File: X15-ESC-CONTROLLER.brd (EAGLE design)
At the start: 100 x 80 mm, 25 parts, among them IC1 OP-AMP, J1 3V3 -SWCLK-GND-SWDIO- NRST, Y1 ECS-80-S-4X

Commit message: Board dimensions
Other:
- board size 100 x 80 mm -> 51.6 x 34.2 mm
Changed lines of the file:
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@@
 <setting verticaltext="up"/>
 </settings>
-<grid distance="50" unitdist="mil" unit="mil" style="lines" multiple="1" display="no" altdistance="5" altunitdist="mil" altunit="mil"/>
+<grid distance="1" unitdist="mil" unit="mil" style="lines" multiple="1" display="no" altdistance="5" altunitdist="mil" altunit="mil"/>
 <layers>
 <layer number="1" name="Top" color="4" fill="1" visible="yes" active="yes"/>
@@
 <board>
 <plain>
-<wire x1="0" y1="0" x2="100" y2="0" width="0" layer="20"/>
-<wire x1="100" y1="0" x2="100" y2="80" width="0" layer="20"/>
-<wire x1="100" y1="80" x2="0" y2="80" width="0" layer="20"/>
-<wire x1="0" y1="80" x2="0" y2="0" width="0" layer="20"/>
+<wire x1="0" y1="0" x2="51.562" y2="0" width="0" layer="20"/>
+<wire x1="51.562" y1="0" x2="51.6382" y2="34.1884" width="0" layer="20"/>
+<wire x1="51.6382" y1="34.1884" x2="0" y2="34.2138" width="0" layer="20"/>
+<wire x1="0" y1="34.2138" x2="0" y2="0" width="0" layer="20"/>
 </plain>
 <attributes>

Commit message: Board Edits
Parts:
- removed LED1: LAP4-BOTTOM, led:P47F-BOTTOM
- removed S1: MOMENTARY-SWITCH-SPST-PTH-6.0MM, SparkFun-Switches:TACTILE_SWITCH_PTH_6.0MM
- added D1: COLOR, LED, 0805:0805
- added J2, J4: (no value), SparkFun-Connectors:1X06_NO_SILK
- added U$7: (no value), OTHER, Push button - FSM2JMTR:DISCRETECOMPONENTS_SW_2512
- J1: device X15-Parts-Library:1X05 -> X15-ESC-Controller-Parts-Library:1X05
- J3: device SparkFun-Connectors:1X10 -> SparkFun-Connectors:1X06_NO_SILK
- U$1: device X15-Parts-Library:STM32F042K6T6 -> X15-ESC-Controller-Parts-Library:STM32F042K6T6
- U$2: device X15-Parts-Library:TCAN337D -> X15-ESC-Controller-Parts-Library:TCAN337D
- U$3, U$4, U$6: device X15-Parts-Library:JST_8_PIN -> X15-ESC-Controller-Parts-Library:JST_8_PIN
- U$5: device X15-Parts-Library:BACKPLANE_CONNECTOR -> X15-ESC-Controller-Parts-Library:BACKPLANE_CONNECTORS_BKP
- Y1: device X15-Parts-Library:XTAL_ECS-80-S-4X -> X15-ESC-Controller-Parts-Library:XTAL_ECS-80-S-4X
- moved JP1 91.1 mm to (46.5, 23.4)
- moved U$2 84.7 mm to (43.9, 8.78)
- moved Y1 74.6 mm to (35.9, 5.23)
- moved C3 72.9 mm to (9.40, 2.79)
- moved U$5 72.0 mm to (42.7, 29.2), turned to 90 degrees
- moved U$1 71.5 mm to (23.8, 23.9)
- moved IC1 69.3 mm to (47.5, 17.3)
- moved C2 68.0 mm to (9.40, 5.84)
- moved C8 67.2 mm to (10.9, 11.4)
- moved R4 65.4 mm to (15.2, 8.13)
- moved U$4 64.0 mm to (41.4, 24.3)
- moved C1 63.2 mm to (9.40, 8.89)
- moved C7 63.1 mm to (8.38, 11.4)
- moved R5 60.3 mm to (9.65, 14.0)
- moved J3 59.5 mm to (3.05, 2.79), turned to 90 degrees
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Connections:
- removed net ADC: J3.1
- removed net N$1: C1.1, C2.1, U$1.VDD
- removed net N$5: C5.2, U$2.VCC
- removed net TIM1_CH4: J3.6
- removed net TIM1_CH5: J3.7
- removed net TIM1_CH6: J3.8
- removed net TIM1_CH7: J3.9
- removed net TIM1_CH8: J3.10
- net +3V3: now also C1.1, C2.1, C5.2, U$1.VDD, U$2.VCC
- net ADC_IN0: now also J4.1
- net ADC_IN1: now also J3.1
- net ADC_IN4: now also J2.1
- net GND: now also D1.C, U$7.1; no longer LED1.C, S1.1
- net N$2: now also U$7.2; no longer S1.3
- net N$8: now also D1.A; no longer LED1.A
- net TIM16_CH1: now also J2.3
- net TIM17_CH1: now also J4.6
- net TIM1_CH1: now also J4.3; no longer J3.3
- net TIM1_CH2: no longer J3.4
- net TIM1_CH3: now also J4.5; no longer J3.5
- net TIM2_CH1: now also J3.3
- net TIM2_CH2: now also J3.4, J4.4
- net TIM2_CH3: now also J3.5
- net TIM2_CH4: now also J3.6
- net TIM3_CH2: now also J2.4
- net TIM3_CH3: now also J2.5
- net TIM3_CH4: now also J2.6
- net TLM_1: now also J4.2
- net TLM_2: now also J3.2
- net TLM_3: now also J2.2
- net TLM_ESC: no longer J3.2
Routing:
- net TIM3_CH4: track 0.00 -> 8.61 mm
- net TIM3_CH3: track 0.00 -> 6.22 mm
- added copper zone on layer 1, net GND
- added copper zone on layer 16, net GND

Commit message: Intermediate Board
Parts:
- moved Y1 1.05 mm to (36.2, 4.21)
- moved J3 0.57 mm to (2.54, 3.05)
- moved J4 0.36 mm to (7.11, 31.8)
- moved U$7 0.25 mm to (23.9, 3.81)
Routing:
- net TIM2_CH1: track 0.00 -> 146.6 mm, vias 0 -> 3
- net +3V3: track 0.00 -> 79.9 mm, vias 0 -> 3
- net TIM3_CH3: track 6.22 -> 82.1 mm, vias 0 -> 5
- net TLM_2: track 0.00 -> 75.3 mm, vias 0 -> 7
- net TIM2_CH2: track 0.00 -> 75.3 mm, vias 0 -> 8
- net GND: track 0.00 -> 73.9 mm, vias 0 -> 11
- net TIM2_CH4: track 0.00 -> 69.1 mm, vias 0 -> 5
- net ADC_IN1: track 0.00 -> 65.7 mm, vias 0 -> 6
- net N$2: track 0.00 -> 56.2 mm, vias 0 -> 4
- net N$4: track 0.00 -> 53.5 mm, vias 0 -> 6
- net TIM16_CH1: track 0.00 -> 49.5 mm, vias 0 -> 2
- net ADC_IN0: track 0.00 -> 48.7 mm, vias 0 -> 2
- net TIM1_CH3: track 0.00 -> 48.4 mm, vias 0 -> 1
- net TIM3_CH2: track 0.00 -> 48.0 mm, vias 0 -> 3
- net TLM_3: track 0.00 -> 47.1 mm, vias 0 -> 6
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
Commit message: Board Traces Completed
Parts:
- moved R3 12.6 mm to (9.37, 4.95)
- moved C4 1.24 mm to (11.2, 28.7)
- moved C2 1.22 mm to (9.37, 7.06)
- moved C8 0.18 mm to (11.0, 11.3)
- moved IC1 0.14 mm to (47.4, 17.3)
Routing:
- net GND: track 73.9 -> 194.4 mm, vias 11 -> 26
- net +3V3: track 79.9 -> 132.2 mm, vias 3 -> 13
- net TIM2_CH3: track 28.0 -> 56.8 mm, vias 4 -> 5
- net N$4: track 53.5 -> 65.9 mm
- net TLM_2: track 75.3 -> 66.1 mm, vias 7 -> 10
- net N$3: track 42.8 -> 51.3 mm
- net TIM1_CH3: track 48.4 -> 56.6 mm
- net N$8: track 0.00 -> 7.38 mm
- net N$2: track 56.2 -> 62.4 mm
- net TIM3_CH2: track 48.0 -> 53.7 mm, vias 3 -> 2
- net TIM16_CH1: track 49.5 -> 53.7 mm
- net TLM_1: track 39.1 -> 42.3 mm
- net TIM3_CH4: track 36.8 -> 39.7 mm
- net SWDIO: track 31.2 -> 33.8 mm
- net ADC_IN1: track 65.7 -> 68.2 mm
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
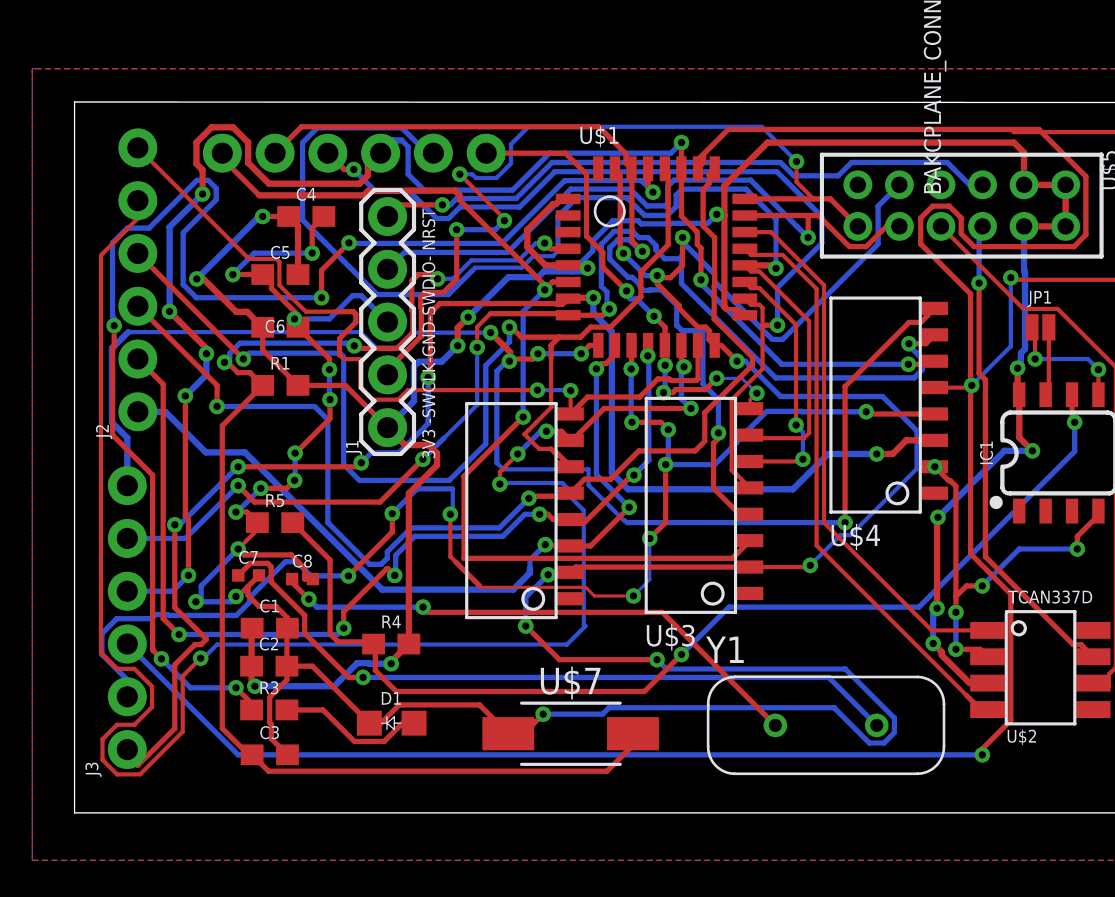
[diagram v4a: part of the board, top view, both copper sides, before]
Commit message: FIxed DRC
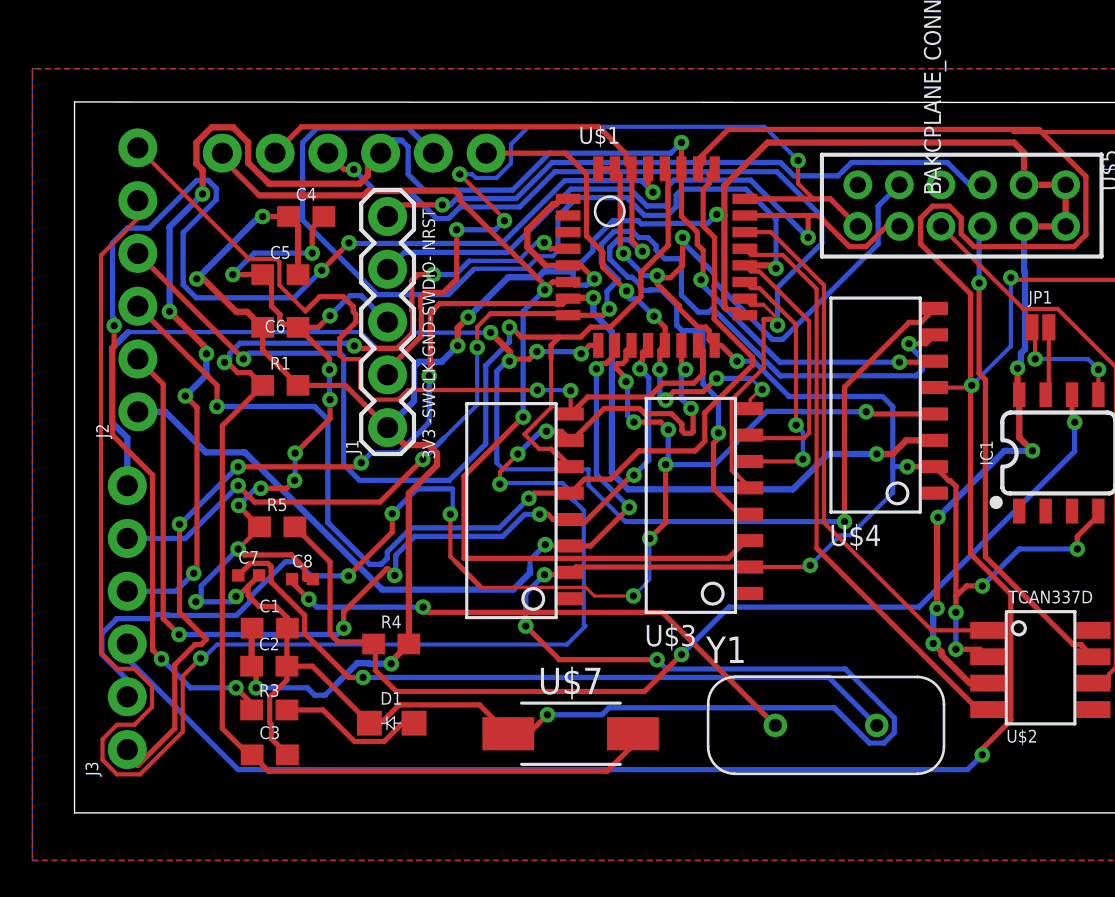
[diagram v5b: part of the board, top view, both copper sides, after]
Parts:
- moved R5 0.23 mm to (9.75, 13.8)
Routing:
- net TIM3_CH3: track 83.8 -> 85.8 mm
- net +3V3: track 132.2 -> 134.1 mm
- net TIM17_CH1: track 23.6 -> 24.8 mm
- net TIM2_CH1: track 146.6 -> 147.6 mm
- net N$4: track 65.9 -> 65.0 mm
- net TIM1_CH1: track 44.4 -> 45.2 mm
- net TIM2_CH3: track 56.8 -> 57.4 mm
- net TLM_2: track 66.1 -> 66.6 mm
- net TIM3_CH4: track 39.7 -> 40.2 mm
- net TIM2_CH2: track 75.4 -> 75.9 mm

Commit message: Final Board Edits
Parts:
- removed J4: (no value), SparkFun-Connectors:1X06_NO_SILK
- added D2: COLOR, LED, 0805:0805
- added R2: 150, SparkFun-Resistors:0603
- U$3, U$4, U$6: device X15-ESC-Controller-Parts-Library:JST_8_PIN -> X15-Parts-Library:8PIN_CONNECTOR
- moved U$4 22.3 mm to (41.6, 1.93), turned to 90 degrees
- moved U$6 17.9 mm to (28.8, 1.94), turned to 90 degrees
- moved U$3 17.1 mm to (49.5, 17.2), turned to 180 degrees
- moved U$2 14.3 mm to (44.7, 23.1)
- moved Y1 9.37 mm to (34.5, 13.4)
- moved U$7 9.28 mm to (21.1, 12.6)
- moved IC1 8.87 mm to (40.3, 22.7)
- moved JP1 2.23 mm to (48.2, 24.7)
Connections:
- removed net TLM_1: J4.2, U$1.PB7, U$3.4
- removed net TLM_2: J3.2, U$1.PA5, U$4.4
- removed net TLM_3: J2.2, U$1.PA6, U$6.4
- new net N$1: D2.A, R2.2
- net +3V3: now also R2.1
- net ADC_IN0: no longer J4.1
- net GND: now also D2.C
- net TIM17_CH1: no longer J4.6
- net TIM1_CH1: no longer J4.3
- net TIM1_CH3: no longer J4.5
- net TIM2_CH2: no longer J4.4
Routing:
- net TLM_2: track 66.6 -> 0.00 mm, vias 10 -> 0
- net TLM_3: track 47.6 -> 0.00 mm, vias 6 -> 0
- net TLM_1: track 42.3 -> 0.00 mm, vias 2 -> 0
- net TIM2_CH1: track 147.6 -> 109.7 mm, vias 3 -> 5
- net TIM1_CH3: track 56.3 -> 29.4 mm, vias 1 -> 0
- net TIM1_CH1: track 45.2 -> 19.6 mm, vias 2 -> 0
- net TIM2_CH3: track 57.4 -> 72.9 mm, vias 5 -> 7
- net TLM: track 3.31 -> 18.1 mm, vias 0 -> 4
- net CAN_L: track 27.5 -> 13.5 mm
- net TIM3_CH4: track 40.2 -> 52.9 mm
- net TLM_ESC: track 6.06 -> 18.6 mm
- net TIM17_CH1: track 24.8 -> 37.2 mm, vias 6 -> 4
- net CAN_H: track 23.3 -> 10.9 mm
- net CAN_RX: track 28.2 -> 16.0 mm
- net TIM1_CH2: track 12.5 -> 24.5 mm
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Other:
- board text added: "Akhilesh Prasad"
- board text added: "Bryce Sasser"
- board text added: "C:/Users/pakhi/Downloads/purduee.bmp"
- board text added: "Katherine Sandys"

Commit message: Hopeful Final Push
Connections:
- net TLM renamed N$10
- net TLM_ESC renamed N$5
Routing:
- net N$10: track 18.1 -> 13.8 mm, vias 4 -> 2
- net GND: track 197.9 -> 193.8 mm
- net +3V3: track 138.2 -> 141.2 mm
- net TIM2_CH4: track 57.2 -> 54.7 mm, vias 6 -> 8
- net TIM3_CH3: track 78.8 -> 80.3 mm
- net N$5: track 18.6 -> 20.0 mm, vias 2 -> 4
- net CAN_L: track 13.5 -> 12.2 mm, vias 0 -> 2
- net CAN_H: track 10.9 -> 12.1 mm
- net N$2: track 68.8 -> 67.7 mm
- net TIM2_CH3: track 72.9 -> 71.8 mm
- net SWCLK: track 39.6 -> 38.8 mm, vias 4 -> 2
- net TIM2_CH2: track 86.1 -> 86.8 mm
- net TIM3_CH2: track 64.0 -> 63.3 mm
- net TIM3_CH4: track 52.9 -> 53.6 mm
- net SWDIO: track 30.8 -> 30.2 mm
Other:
- board text added: "Minh Nguyen"
- board text added: "POWER LED"
- board text added: "Rachel Livesay"
- board text added: "TIMER CHANNEL TEST POINTS"
- board text removed: "C:/Users/pakhi/Downloads/purduee.bmp"
